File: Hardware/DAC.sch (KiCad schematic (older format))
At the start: 10 parts, among them U11 PCM1796

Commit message: routing digital signal wires
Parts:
- C47: footprint Capacitors_SMD:c_elec_4x4.5 -> Capacitors_SMD:C_1206
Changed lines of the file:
@@
 F 0 "C47" H 8000 3050 40  0000 L CNN
 F 1 "10uF" H 8006 2865 40  0000 L CNN
-F 2 "Capacitors_SMD:c_elec_4x4.5" H 8038 2800 30  0001 C CNN
+F 2 "Capacitors_SMD:C_1206" H 8038 2800 30  0001 C CNN
 F 3 "" H 8000 2950 60  0000 C CNN
 	1    8000 2950
@@
 NoConn ~ 5700 3850
 $Comp
-L +3.3VSB #PWR075
+L +3.3VSB #PWR073
 U 1 1 57F8A593
 P 2800 4500
-F 0 "#PWR075" H 2800 4460 30  0001 C CNN
+F 0 "#PWR073" H 2800 4460 30  0001 C CNN
 F 1 "+3.3VSB" H 2800 4610 30  0000 C CNN
 F 2 "" H 2800 4500 60  0000 C CNN
@@
 ANALOG_OUT_R
 $Comp
-L +3.3VSB #PWR076
+L +3.3VSB #PWR074
 U 1 1 5859BC27
 P 8150 2600
-F 0 "#PWR076" H 8150 2560 30  0001 C CNN
+F 0 "#PWR074" H 8150 2560 30  0001 C CNN
 F 1 "+3.3VSB" H 8150 2710 30  0000 C CNN
 F 2 "" H 8150 2600 60  0000 C CNN
@@
 $EndComp
 $Comp
-L +5V #PWR?
+L +5V #PWR075
 U 1 1 58614BD8
 P 2800 3300
-F 0 "#PWR?" H 2800 3390 20  0001 C CNN
+F 0 "#PWR075" H 2800 3390 20  0001 C CNN
 F 1 "+5V" H 2800 3390 30  0000 C CNN
 F 2 "" H 2800 3300 60  0000 C CNN
@@
 $EndComp
 $Comp
-L +5V #PWR?
+L +5V #PWR076
 U 1 1 58614C2C
 P 7100 2600
-F 0 "#PWR?" H 7100 2690 20  0001 C CNN
+F 0 "#PWR076" H 7100 2690 20  0001 C CNN
 F 1 "+5V" H 7100 2690 30  0000 C CNN
 F 2 "" H 7100 2600 60  0000 C CNN
@@
 $EndComp
 $Comp
-L +5V #PWR?
+L +5V #PWR077
 U 1 1 58614C79
 P 5800 3300
-F 0 "#PWR?" H 5800 3390 20  0001 C CNN
+F 0 "#PWR077" H 5800 3390 20  0001 C CNN
 F 1 "+5V" H 5800 3390 30  0000 C CNN
 F 2 "" H 5800 3300 60  0000 C CNN

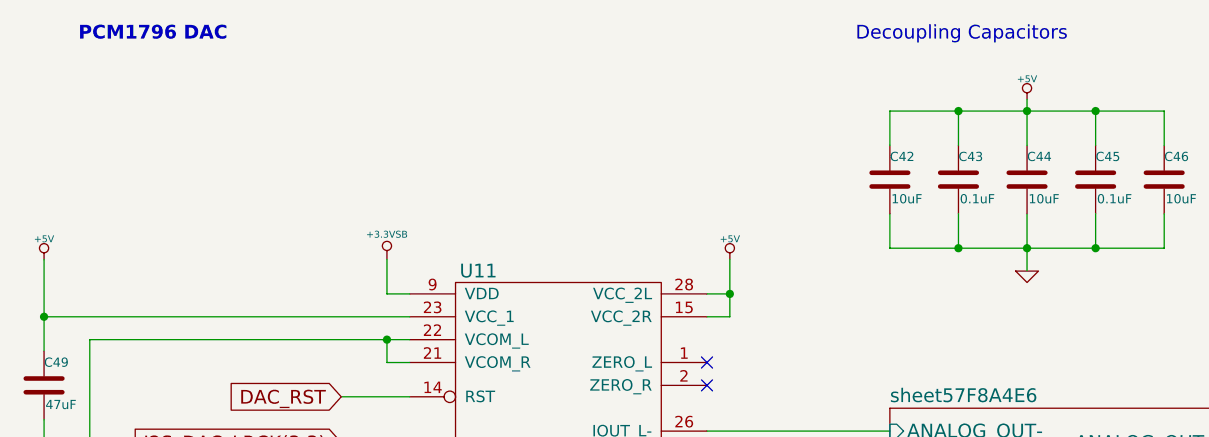
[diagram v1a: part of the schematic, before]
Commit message: Digital Half completed placement
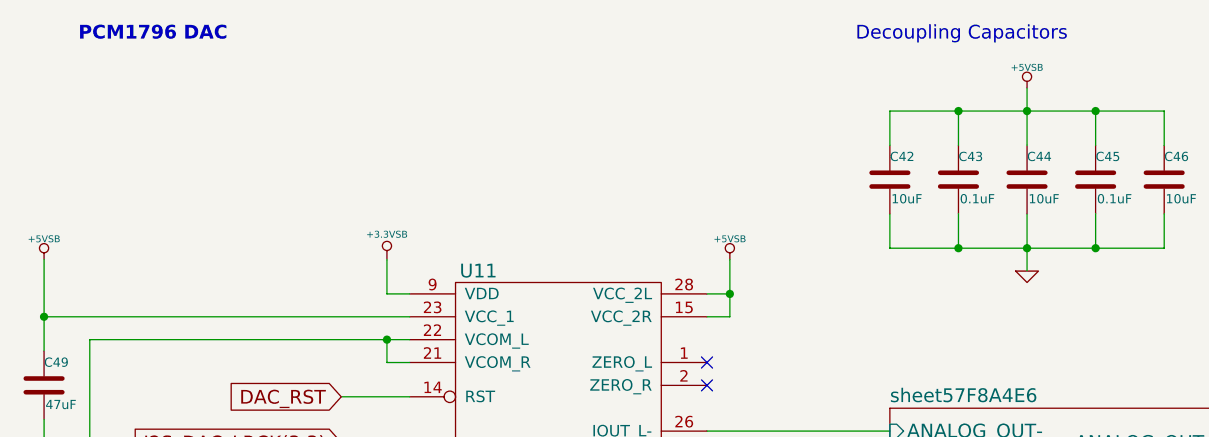
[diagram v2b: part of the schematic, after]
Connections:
- net +5V renamed +5VSB
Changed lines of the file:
@@
 Pulled HIGH for\nI2C mode
 $Comp
-L GND-RESCUE-museV2-RESCUE-museV2 #PWR068
+L GND-RESCUE-museV2-RESCUE-museV2 #PWR065
 U 1 1 57F8A4EE
 P 8150 3350
-F 0 "#PWR068" H 8150 3350 30  0001 C CNN
+F 0 "#PWR065" H 8150 3350 30  0001 C CNN
 F 1 "GND" H 8150 3280 30  0001 C CNN
 F 2 "" H 8150 3350 60  0000 C CNN
@@
 Decoupling Capacitors
 $Comp
-L GND-RESCUE-museV2-RESCUE-museV2 #PWR069
+L GND-RESCUE-museV2-RESCUE-museV2 #PWR066
 U 1 1 57F8A50F
 P 7100 3350
-F 0 "#PWR069" H 7100 3350 30  0001 C CNN
+F 0 "#PWR066" H 7100 3350 30  0001 C CNN
 F 1 "GND" H 7100 3280 30  0001 C CNN
 F 2 "" H 7100 3350 60  0000 C CNN
@@
 $EndComp
 $Comp
-L GND-RESCUE-museV2-RESCUE-museV2 #PWR070
+L GND-RESCUE-museV2-RESCUE-museV2 #PWR067
 U 1 1 57F8A564
 P 6100 5450
-F 0 "#PWR070" H 6100 5450 30  0001 C CNN
+F 0 "#PWR067" H 6100 5450 30  0001 C CNN
 F 1 "GND" H 6100 5380 30  0001 C CNN
 F 2 "" H 6100 5450 60  0000 C CNN
@@
 $EndComp
 $Comp
-L GND-RESCUE-museV2-RESCUE-museV2 #PWR071
+L GND-RESCUE-museV2-RESCUE-museV2 #PWR068
 U 1 1 57F8A571
 P 5800 5450
-F 0 "#PWR071" H 5800 5450 30  0001 C CNN
+F 0 "#PWR068" H 5800 5450 30  0001 C CNN
 F 1 "GND" H 5800 5380 30  0001 C CNN
 F 2 "" H 5800 5450 60  0000 C CNN
@@
 PCM1796 DAC
 $Comp
-L +3.3VSB #PWR072
+L +3.3VSB #PWR069
 U 1 1 57F8A57F
 P 4300 3300
-F 0 "#PWR072" H 4300 3260 30  0001 C CNN
+F 0 "#PWR069" H 4300 3260 30  0001 C CNN
 F 1 "+3.3VSB" H 4300 3410 30  0000 C CNN
 F 2 "" H 4300 3300 60  0000 C CNN
@@
 NoConn ~ 5700 3850
 $Comp
-L +3.3VSB #PWR073
+L +3.3VSB #PWR070
 U 1 1 57F8A593
 P 2800 4500
-F 0 "#PWR073" H 2800 4460 30  0001 C CNN
+F 0 "#PWR070" H 2800 4460 30  0001 C CNN
 F 1 "+3.3VSB" H 2800 4610 30  0000 C CNN
 F 2 "" H 2800 4500 60  0000 C CNN
@@
 	7950 4100 8250 4100
 Wire Wire Line
-	7100 2600 7100 2800
-Wire Wire Line
 	6500 2650 7700 2650
 Wire Wire Line
@@
 ANALOG_OUT_R
 $Comp
-L +3.3VSB #PWR074
+L +3.3VSB #PWR071
 U 1 1 5859BC27
 P 8150 2600
-F 0 "#PWR074" H 8150 2560 30  0001 C CNN
+F 0 "#PWR071" H 8150 2560 30  0001 C CNN
 F 1 "+3.3VSB" H 8150 2710 30  0000 C CNN
 F 2 "" H 8150 2600 60  0000 C CNN
@@
 $EndComp
 $Comp
-L +5V #PWR075
-U 1 1 58614BD8
+L +5VSB #PWR072
+U 1 1 58670EE1
 P 2800 3300
-F 0 "#PWR075" H 2800 3390 20  0001 C CNN
-F 1 "+5V" H 2800 3390 30  0000 C CNN
+F 0 "#PWR072" H 2800 3390 20  0001 C CNN
+F 1 "+5VSB" H 2800 3390 30  0000 C CNN
 F 2 "" H 2800 3300 60  0000 C CNN
 F 3 "" H 2800 3300 60  0000 C CNN
@@
 $EndComp
 $Comp
-L +5V #PWR076
-U 1 1 58614C2C
-P 7100 2600
-F 0 "#PWR076" H 7100 2690 20  0001 C CNN
-F 1 "+5V" H 7100 2690 30  0000 C CNN
-F 2 "" H 7100 2600 60  0000 C CNN
-F 3 "" H 7100 2600 60  0000 C CNN
-	1    7100 2600
-	1    0    0    -1
-$EndComp
-$Comp
-L +5V #PWR077
-U 1 1 58614C79
+L +5VSB #PWR073
+U 1 1 58671B83
 P 5800 3300
-F 0 "#PWR077" H 5800 3390 20  0001 C CNN
-F 1 "+5V" H 5800 3390 30  0000 C CNN
+F 0 "#PWR073" H 5800 3390 20  0001 C CNN
+F 1 "+5VSB" H 5800 3390 30  0000 C CNN
 F 2 "" H 5800 3300 60  0000 C CNN
 F 3 "" H 5800 3300 60  0000 C CNN
@@
 	1    0    0    -1
 $EndComp
+$Comp
+L +5VSB #PWR074
+U 1 1 5867214D
+P 7100 2550
+F 0 "#PWR074" H 7100 2640 20  0001 C CNN
+F 1 "+5VSB" H 7100 2640 30  0000 C CNN
+F 2 "" H 7100 2550 60  0000 C CNN
+F 3 "" H 7100 2550 60  0000 C CNN
+	1    7100 2550
+	1    0    0    -1
+$EndComp
+Wire Wire Line
+	7100 2800 7100 2550
 $EndSCHEMATC
